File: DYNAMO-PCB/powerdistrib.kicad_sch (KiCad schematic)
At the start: 8 parts, among them J19 USB3_A, J20 USB3_A, J26 USB_C_Receptacle_USB2.0_16P, J27 USB_C_Receptacle_USB2.0_16P, J28 USB_C_Receptacle_USB2.0_16P, J30 USB_C_Receptacle_USB2.0_16P

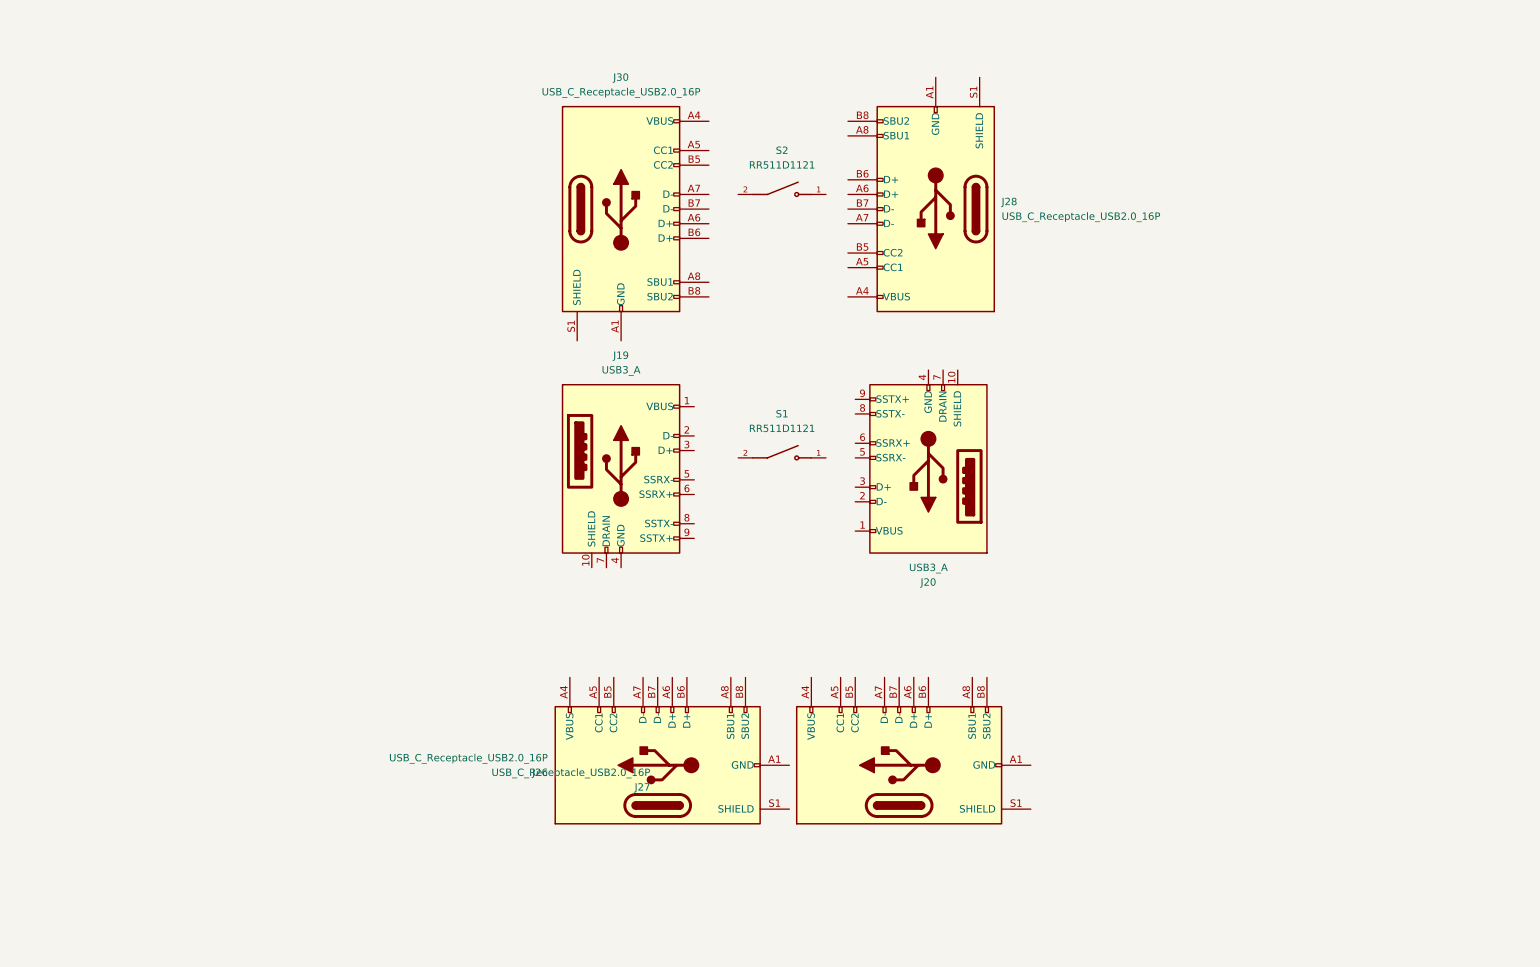
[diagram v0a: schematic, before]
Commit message: removed unncessary ic
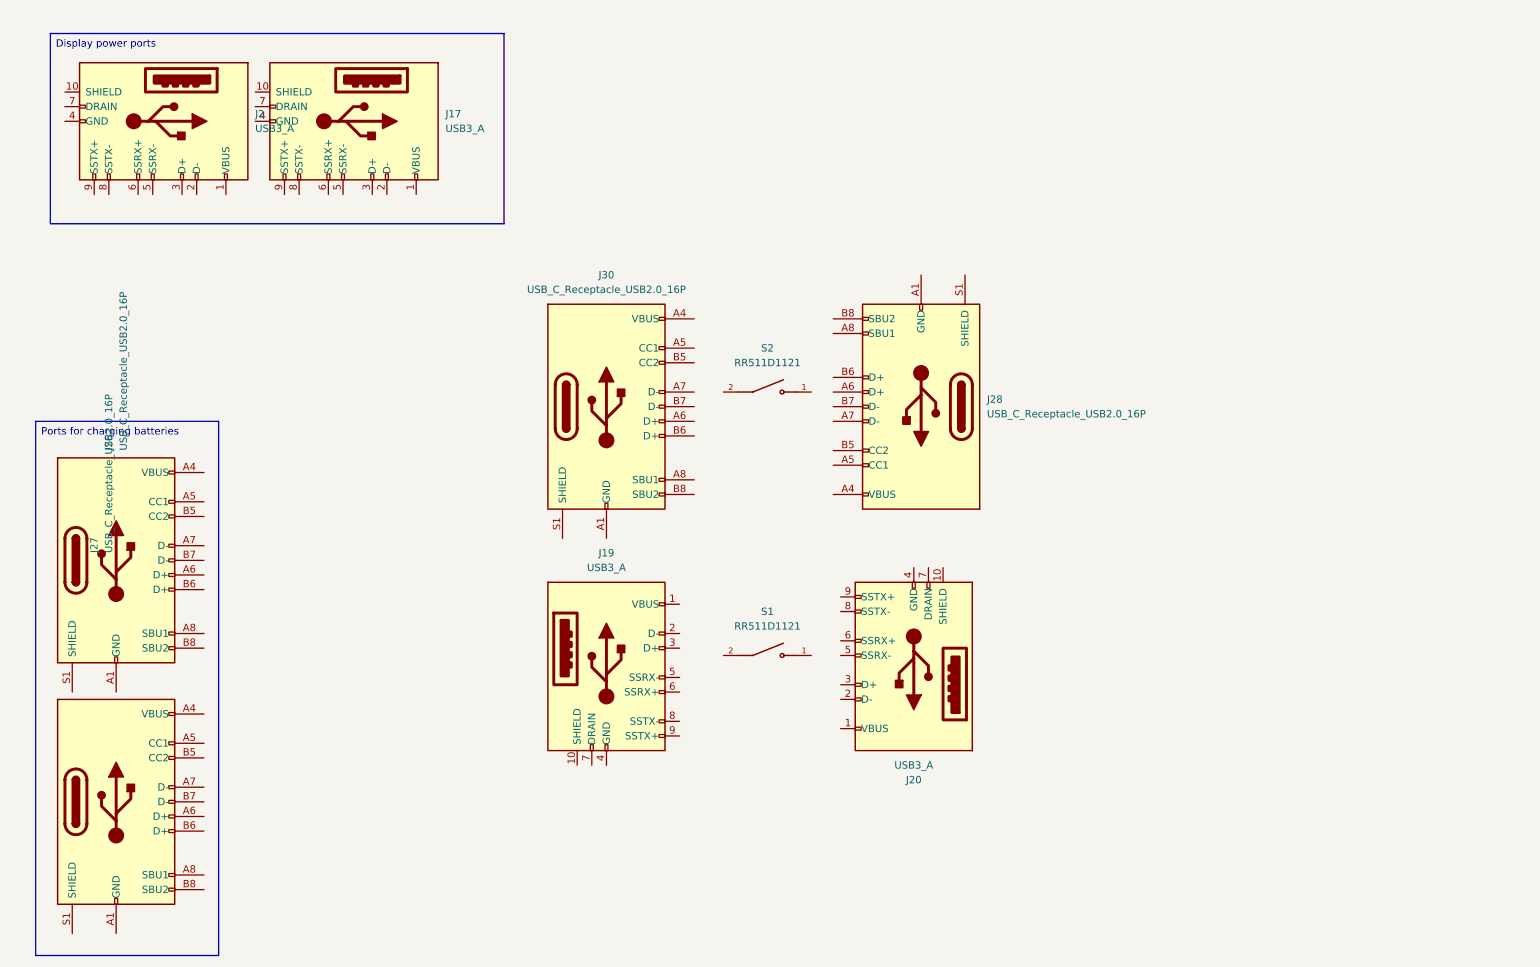
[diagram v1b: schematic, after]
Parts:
- added J17, J2: USB3_A, 692122030100:692122030100, symbol Connector:USB3_A
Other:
- moved on the sheet: J19, J20, J26, J27, J28, J30, S1, S2

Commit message: schematic wip
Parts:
- removed J20: USB3_A, 692122030100:692122030100, symbol Connector:USB3_A
- removed J26, J27, J28, J30: USB_C_Receptacle_USB2.0_16P, Connector_USB:USB_C_Receptacle_GCT_USB4105-xx-A_16P_TopMnt_Horizontal, symbol Connector:USB_C_Receptacle_USB2.0_16P
- added J14, J15, J26, J4: USB_C_Receptacle_PowerOnly_6P, symbol Connector:USB_C_Receptacle_PowerOnly_6P
- added J16: USB_C_Receptacle, symbol Connector:USB_C_Receptacle
- added J31, J32: USB3_A, 692122030100:692122030100, symbol Connector:USB3_A
- added S3: RR511D1121, RR511D1121:E-SWITCH_RR511D1121, symbol RR511D1121:RR511D1121
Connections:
- net +5V peripherals: now reaches S1.1
- net +5V peripherals: now also J17.1 (VBUS), J2.1 (VBUS)
- net at S1.2: now also J19.1 (VBUS)
- net at J19.10 (SHIELD): now also J17.10 (SHIELD), J2.10 (SHIELD)
- net GND: now reaches J19.4 (GND)
- net GND: now also J17.4 (GND), J2.4 (GND), J14.A12 (GND), J14.B12 (GND), J15.A12 (GND), J15.B12 (GND), J16.A1 (GND), J16.A12 (GND), J16.B1 (GND), J16.B12 (GND), J26.A12 (GND), J26.B12 (GND), J31.4 (GND), J32.4 (GND), J4.A12 (GND), J4.B12 (GND)
- net at S2.1: now also J16.A4 (VBUS), J16.A9 (VBUS), J16.B4 (VBUS), J16.B9 (VBUS)
- net at S2.2: now also J26.A9 (VBUS), J26.B9 (VBUS), J4.A9 (VBUS), J4.B9 (VBUS)
- new net: J14.A5 (CC1), J15.A5 (CC1)
- new net: J14.A9 (VBUS), J14.B9 (VBUS), J15.A9 (VBUS), J15.B9 (VBUS)
- new net: J14.B5 (CC2), J15.B5 (CC2)
- new net: J14.S1 (SHIELD), J15.S1 (SHIELD)
- new net: J16.A5 (CC1), J26.A5 (CC1), J4.A5 (CC1)
- new net: J16.B5 (CC2), J26.B5 (CC2), J4.B5 (CC2)
- new net: J16.S1 (SHIELD), J26.S1 (SHIELD), J4.S1 (SHIELD)
- new net: J31.1 (VBUS), S3.2
- new net: J31.10 (SHIELD), J32.10 (SHIELD)
- new net: J31.2 (D-), J32.2 (D-)
- new net: J31.3 (D+), J32.3 (D+)
- new net: J31.5 (SSRX-), J32.5 (SSRX-)
- new net: J31.6 (SSRX+), J32.6 (SSRX+)
- new net: J31.7 (DRAIN), J32.7 (DRAIN)
- new net: J31.8 (SSTX-), J32.8 (SSTX-)
- new net: J31.9 (SSTX+), J32.9 (SSTX+)
- new net: J32.1 (VBUS), S3.1
- no-connect marks 0 -> 21
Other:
- moved on the sheet: J17, J19, J2, S1, S2

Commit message: schematic wip
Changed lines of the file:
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@@
 	(text_box "4G modem port"
 		(exclude_from_sim no)
-		(at 110.49 127 0)
-		(size 80.01 40.64)
+		(at 110.49 125.73 0)
+		(size 80.01 41.91)
 		(margins 0.9525 0.9525 0.9525 0.9525)
 		(stroke
@@
 	)
 	(junction
-		(at 222.25 104.14)
-		(diameter 0)
-		(color 0 0 0 0)
-	)
-	(junction
 		(at 127 102.87)
 		(diameter 0)
@@
 	)
 	(junction
+		(at 222.25 81.28)
+		(diameter 0)
+		(color 0 0 0 0)
+	)
+	(junction
 		(at 147.32 102.87)
 		(diameter 0)
@@
 	(wire
 		(pts
-			(xy 222.25 55.88) (xy 222.25 104.14)
+			(xy 222.25 55.88) (xy 222.25 81.28)
 		)
 		(stroke
@@
 	(wire
 		(pts
+			(xy 222.25 81.28) (xy 222.25 105.41)
+		)
+		(stroke
+			(width 0)
+			(type default)
+		)
+	)
+	(wire
+		(pts
 			(xy 72.39 88.9) (xy 124.46 36.83)
 		)
@@
 	(wire
 		(pts
-			(xy 236.22 77.47) (xy 240.03 77.47)
+			(xy 236.22 77.47) (xy 238.76 77.47)
 		)
 		(stroke
@@
 	(wire
 		(pts
-			(xy 224.79 104.14) (xy 222.25 104.14)
+			(xy 238.76 81.28) (xy 222.25 81.28)
 		)
 		(stroke
@@
 		(pts
 			(xy 134.62 58.42) (xy 138.43 62.23)
-		)
-		(stroke
-			(width 0)
-			(type default)
-		)
-	)
-	(wire
-		(pts
-			(xy 222.25 104.14) (xy 222.25 105.41)
 		)
 		(stroke
@@
 	(hierarchical_label "GND peripherals"
 		(shape input)
-		(at 224.79 104.14 0)
+		(at 238.76 81.28 0)
 		(effects
 			(font

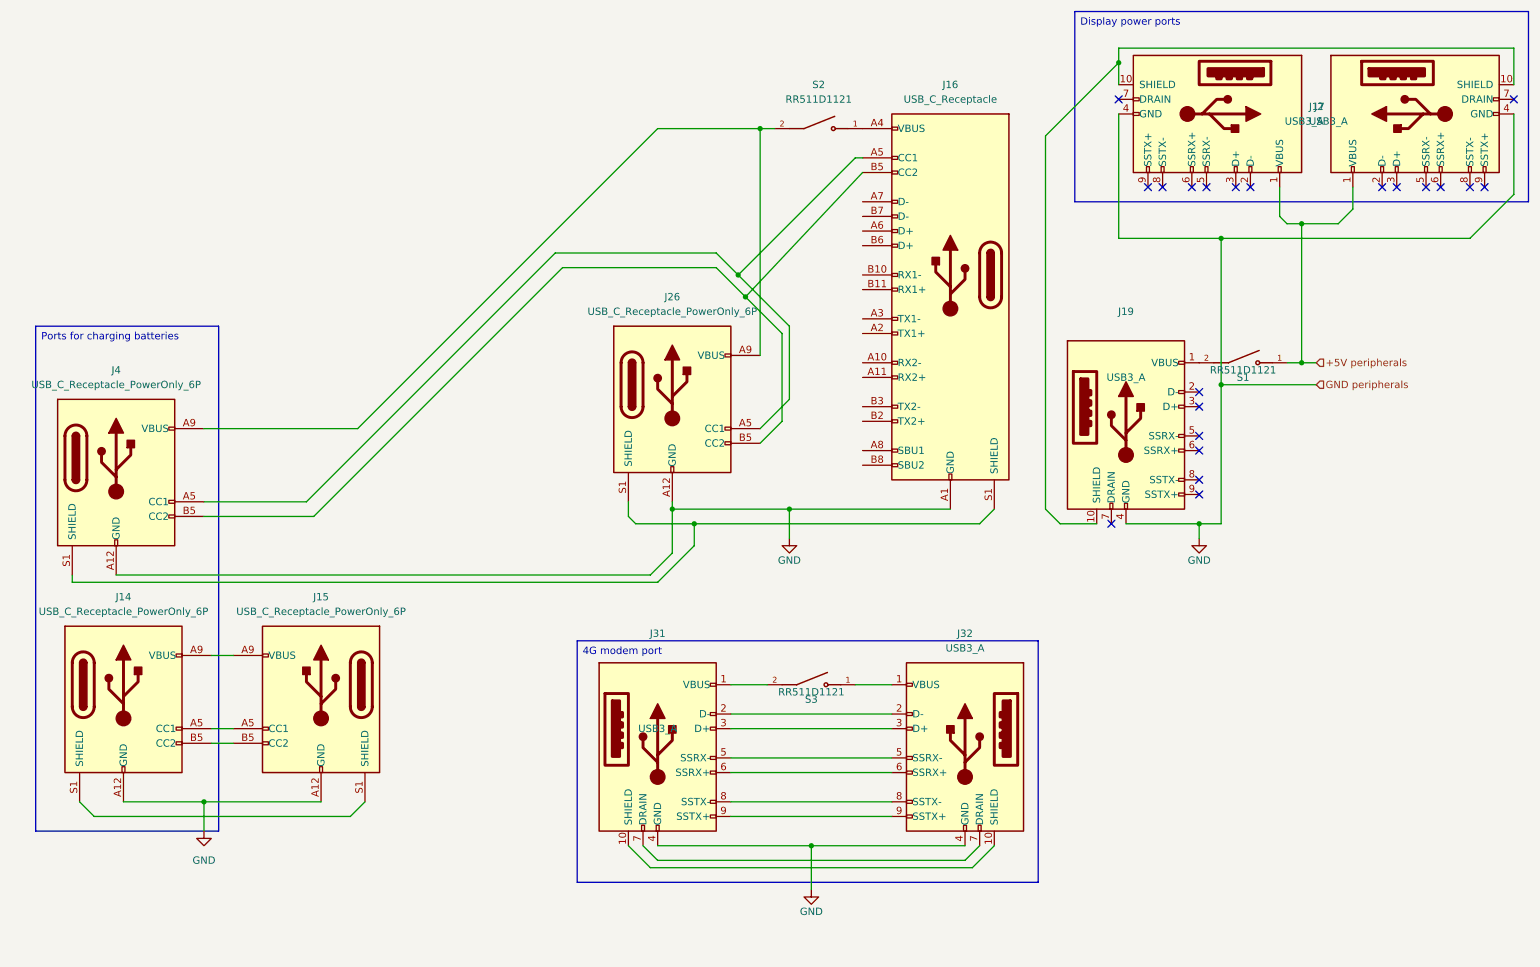
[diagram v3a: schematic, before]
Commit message: schematic complete (pre-ERC)
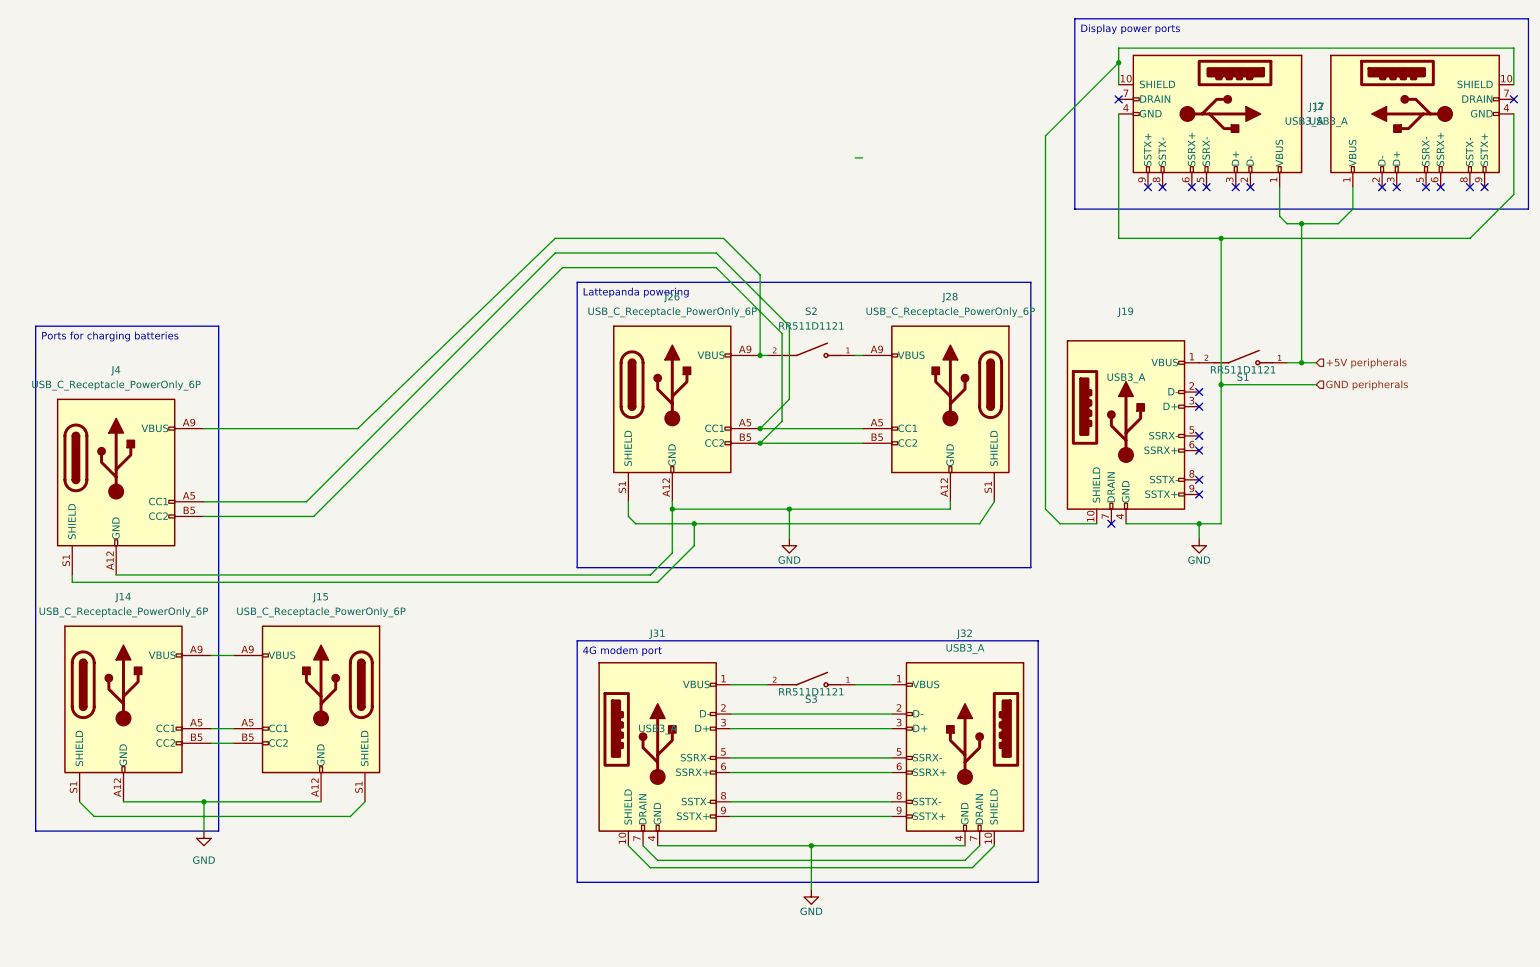
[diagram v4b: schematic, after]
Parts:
- removed J16: USB_C_Receptacle, symbol Connector:USB_C_Receptacle
- added J28: USB_C_Receptacle_PowerOnly_6P, Connector_USB:USB_C_Receptacle_GCT_USB4125-xx-x_6P_TopMnt_Horizontal, symbol Connector:USB_C_Receptacle_PowerOnly_6P
- J14, J15, J26, J4: footprint (none) -> Connector_USB:USB_C_Receptacle_GCT_USB4125-xx-x_6P_TopMnt_Horizontal
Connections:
- net GND: now also J28.A12 (GND), J28.B12 (GND)
- net at J26.A5 (CC1), J4.A5 (CC1): now also J28.A5 (CC1)
- net at J26.B5 (CC2), J4.B5 (CC2): now also J28.B5 (CC2)
- net at J26.S1 (SHIELD), J4.S1 (SHIELD): now also J28.S1 (SHIELD)
- net at S2.1: now also J28.A9 (VBUS), J28.B9 (VBUS)
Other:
- moved on the sheet: S2

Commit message: fix erc errors
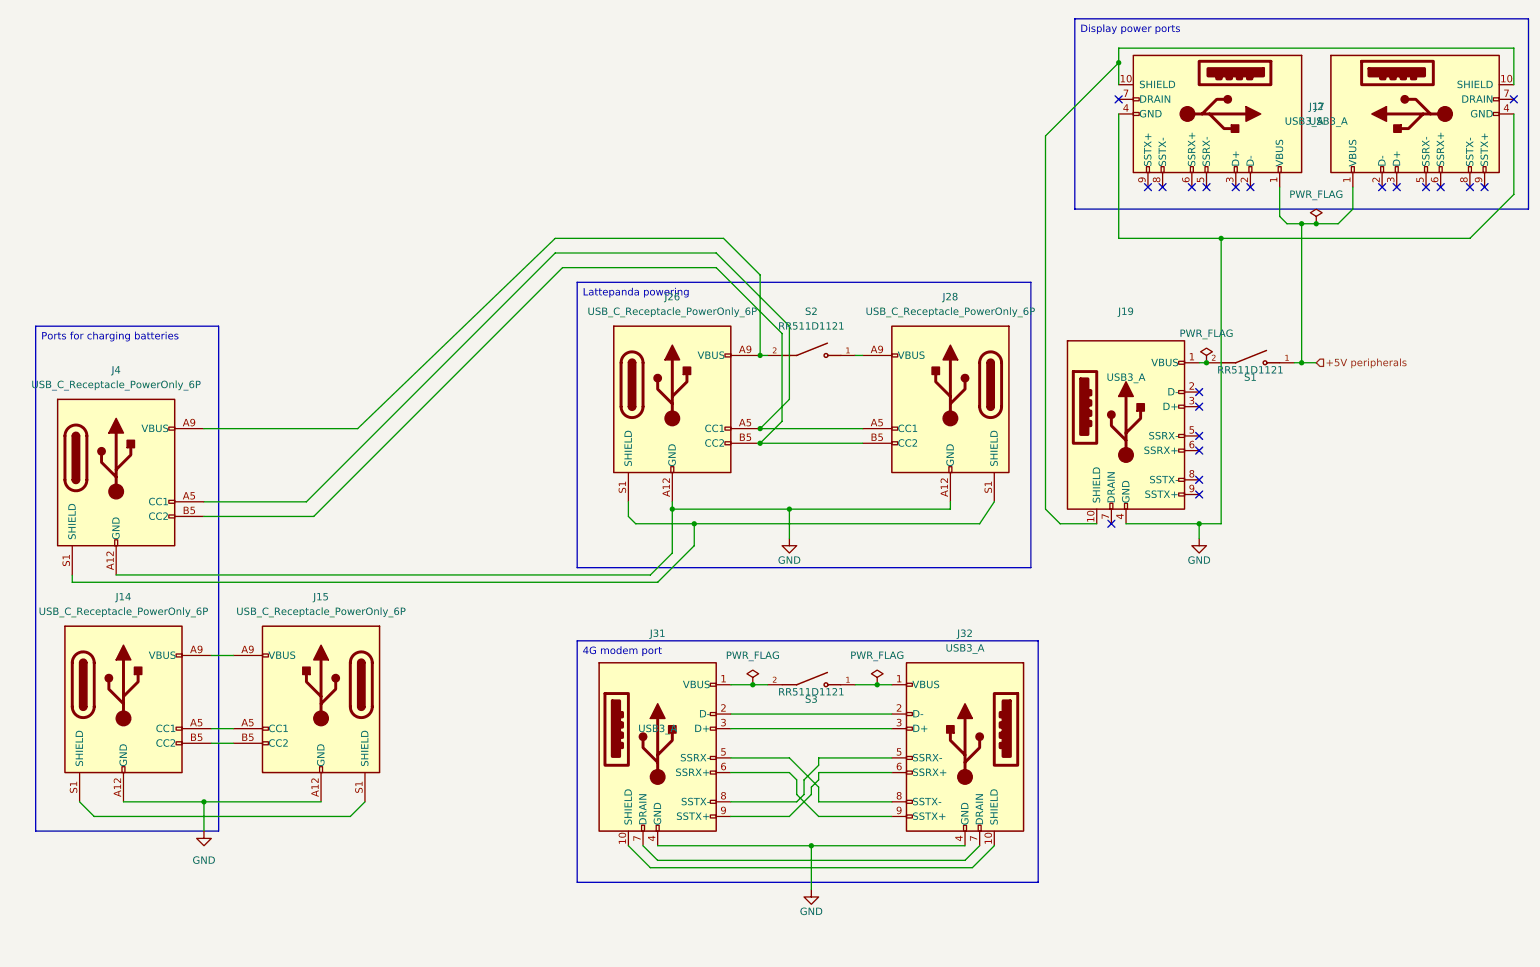
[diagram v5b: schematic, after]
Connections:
- net at J31.5 (SSRX-): now also J32.8 (SSTX-); no longer J32.5 (SSRX-)
- net at J31.6 (SSRX+): now also J32.9 (SSTX+); no longer J32.6 (SSRX+)
- net at J31.8 (SSTX-): now also J32.5 (SSRX-); no longer J32.8 (SSTX-)
- net at J31.9 (SSTX+): now also J32.6 (SSRX+); no longer J32.9 (SSTX+)
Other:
- moved on the sheet: S1
